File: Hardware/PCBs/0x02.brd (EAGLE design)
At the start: 99.4 x 39.4 mm, 42 parts, among them IC1 78L05Z, IC2 TL072, IC3 4050N, SW1 TL2285

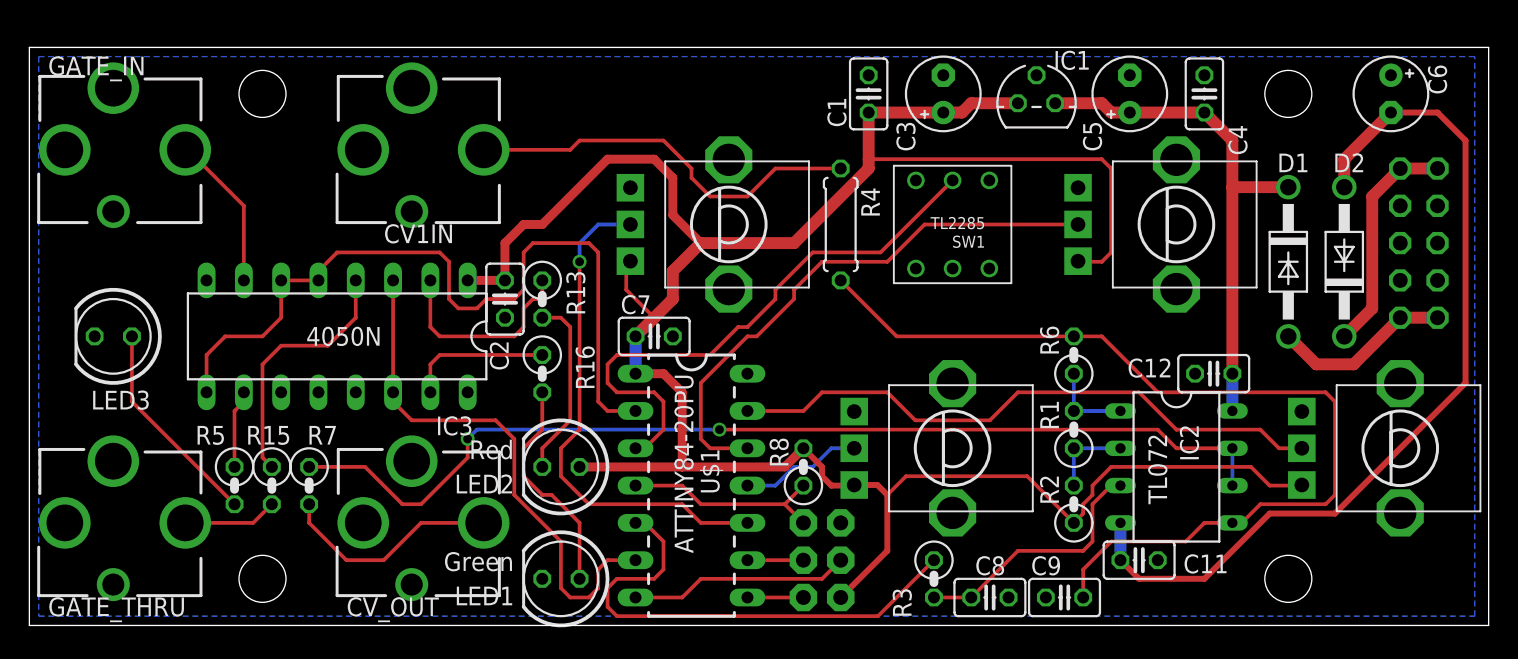
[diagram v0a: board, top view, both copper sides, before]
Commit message: Checkin of code & PCB for version 3 with DAC instead of PWM output.
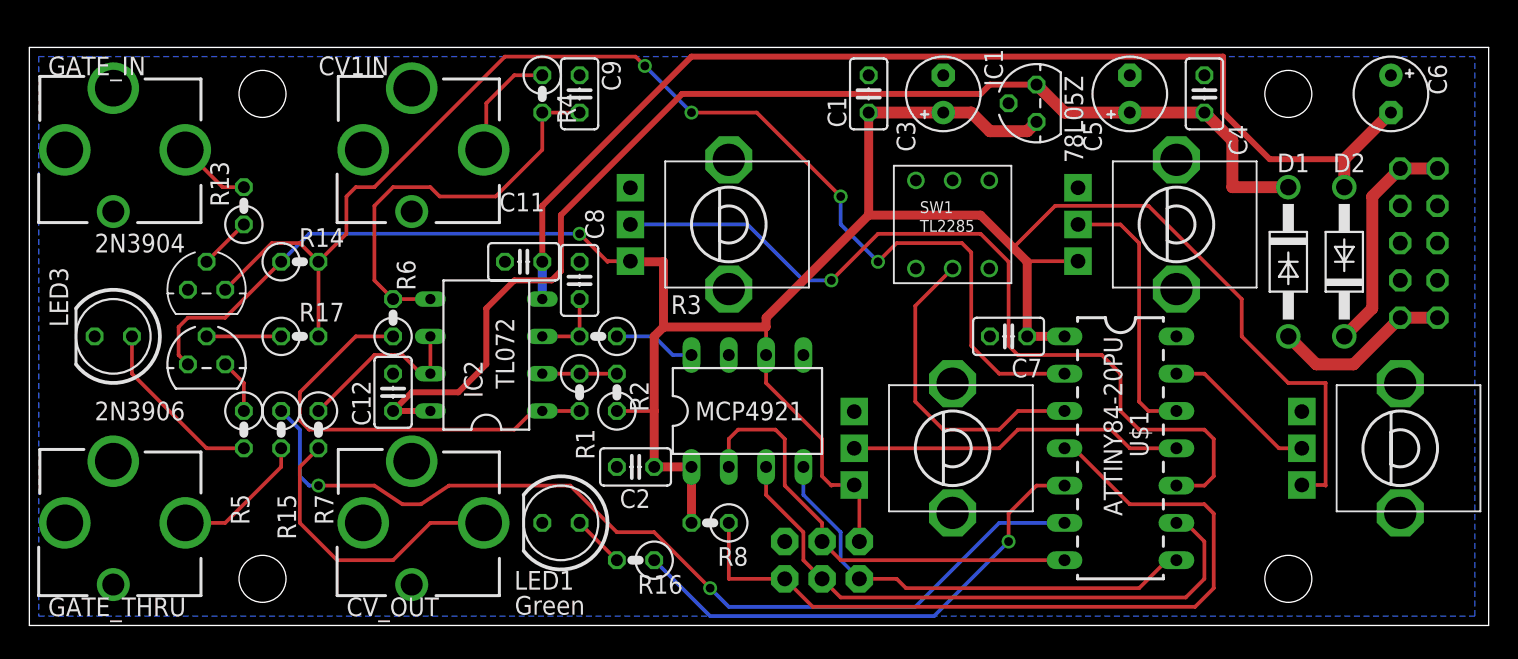
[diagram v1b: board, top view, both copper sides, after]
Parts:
- removed IC3: 4050N, 40xx:DIL16
- removed LED2: Red, led:LED5MM
- added Q1: 2N3906, transistor-pnp:TO92
- added R14: 10k, rcl:0207/2V
- added R17: 100k, rcl:0207/2V
- added T1: 2N3904, transistor:TO92
- added U$3: MCP4921, adafruit_mcp:DIL08
- C8, C9: value 10n -> 470p
- R13: value 1k -> 100k
- R4: device rcl:0207/7 -> rcl:0207/2V
- moved C12 55.9 mm to (25.4, 16.5), turned to 90 degrees
- moved C9 47.6 mm to (38.1, 36.8), turned to 90 degrees
- moved IC2 47.6 mm to (31.8, 19.1), turned to 90 degrees
- moved C11 46.6 mm to (34.3, 25.4), turned to 0 degrees
- moved R6 46.4 mm to (25.4, 21.6)
- moved C8 35.3 mm to (38.1, 24.1), turned to 90 degrees
- moved R1 33.8 mm to (38.1, 16.5), turned to 270 degrees
- moved R2 32.0 mm to (40.6, 16.5)
- moved U$1 29.3 mm to (74.9, 11.4)
- moved R3 28.2 mm to (39.4, 20.3), turned to 180 degrees
- moved C7 24.1 mm to (67.3, 20.3), turned to 180 degrees
- moved R4 22.2 mm to (35.6, 36.8)
- moved R13 21.3 mm to (15.2, 29.2), turned to 90 degrees
- moved C2 14.5 mm to (41.9, 11.4), turned to 180 degrees
- moved R16 14.2 mm to (41.9, 5.08), turned to 180 degrees
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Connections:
- removed net GATE: IC3.5, IC3.6, IC3.9, U$1.2
- removed net MISO: U$1.8, U$2.1
- removed net MOSI: U$1.7, U$2.4
- removed net N$17: IC3.4, R15.1
- removed net N$18: IC3.15, R16.1
- removed net N$20: LED2.K, R13.2
- removed net PWM_B: IC3.14, IC3.3, U$1.6
- new net DAC_OUT: R3.1, U$3.8
- new net GATE_IN: R14.2, R17.2, T1.1, U$1.2
- new net GATE_OUT: R15.1, U$1.6
- new net MISO_DO: U$1.8, U$2.1, U$3.4
- new net MOSI_SS: U$1.7, U$2.4, U$3.2
- new net N$4: Q1.2, R17.1
- net +5V: now also Q1.3, R14.1, U$3.1, U$3.6; no longer IC3.1, LED2.A
- net GND: now also T1.3, U$3.5, U$3.7; no longer IC3.11, IC3.8
- net N$1: now also T1.2; no longer IC3.2
- net N$2: now also Q1.1; no longer IC3.10
- net N$8: now also R13.2; no longer IC3.7
- net PWM_A: now also R16.1; no longer R3.1
- net SCK: now also U$3.3
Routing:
- net GATE_IN: track 0.00 -> 86.2 mm, vias 0 -> 4
- net GATE_OUT: track 0.00 -> 63.9 mm, vias 0 -> 2
- net N$15: track 69.8 -> 12.3 mm, vias 2 -> 0
- net GATE: track 53.6 -> 0.00 mm
- net +12V: track 35.3 -> 81.9 mm
- net RESET: track 14.3 -> 55.2 mm
- net SCK: track 3.81 -> 41.3 mm
- net N$12: track 64.6 -> 28.0 mm
- net PWM_B: track 36.2 -> 0.00 mm
- net MISO_DO: track 0.00 -> 31.8 mm
- net MOSI_SS: track 0.00 -> 31.3 mm
- net PA0: track 41.4 -> 10.6 mm
- net PA3: track 34.4 -> 58.6 mm
- net N$10: track 5.72 -> 29.7 mm
- net PA1: track 37.8 -> 18.3 mm
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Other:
- board text added: "0x02v3"
- board text added: "cc-by-sa 2015 Lars Bengtsson"
- board text removed: "0x02"
- board text removed: "cc-by-sa 2014 Lars Bengtsson"

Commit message: Added jumper to set voltage output range, -5V to +5V or 0-+10V.
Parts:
- added JP2: (no value), pinhead:1X03
- moved C2 1.80 mm to (43.2, 10.2), turned to 270 degrees
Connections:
- new net N$6: JP2.2, R2.1
- net +5V: now also JP2.1; no longer R2.1
- net GND: now also JP2.3
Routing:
- net N$6: track 0.00 -> 3.96 mm
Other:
- board text added: "0x02 3.1 20150320"
- board text added: "Bipolar -5V to +5V"
- board text added: "Unipolar 0V to +10V"
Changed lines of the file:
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@@
 <wire x1="92.71" y1="20.32" x2="92.71" y2="33.02" width="0.254" layer="22" style="shortdash"/>
 <rectangle x1="92.71" y1="33.02" x2="97.79" y2="33.655" layer="22"/>
+<text x="31.115" y="12.7" size="1.27" layer="22" rot="SMR90">Unipolar
+0V to +10V</text>
+<text x="90.17" y="1.905" size="1.27" layer="25">0x02 3.1
+20150320</text>
+<text x="41.91" y="12.7" size="1.27" layer="22" rot="SMR90">Bipolar
+-5V to +5V</text>
 </plain>
 <attributes>
@@
 <attribute name="VALUE" x="18.9992" y="18.0848" size="1.27" layer="27" ratio="10"/>
 </element>
-<element name="C2" library="rcl" package="C025-025X050" value="100n" x="41.91" y="11.43" smashed="yes" rot="R180">
-<attribute name="NAME" x="42.926" y="9.906" size="1.27" layer="25" ratio="10" rot="R180"/>
-<attribute name="VALUE" x="44.196" y="8.509" size="1.27" layer="27" ratio="10" rot="R180"/>
+<element name="C2" library="rcl" package="C025-025X050" value="100n" x="43.18" y="10.16" smashed="yes" rot="R270">
+<attribute name="NAME" x="42.164" y="6.604" size="1.27" layer="25" ratio="10"/>
+<attribute name="VALUE" x="40.386" y="11.176" size="1.27" layer="27" ratio="10" rot="R270"/>
+</element>
+<element name="JP2" library="pinhead" package="1X03" value="" x="38.1" y="12.7" smashed="yes" rot="MR0">
+<attribute name="NAME" x="39.4462" y="9.4488" size="1.27" layer="26" ratio="10" rot="MR0"/>
+<attribute name="VALUE" x="41.91" y="9.525" size="1.27" layer="28" rot="MR0"/>
 </element>
 </elements>
@@
 <contactref element="U$3" pad="5"/>
 <contactref element="C2" pad="2"/>
+<contactref element="JP2" pad="3"/>
 </signal>
 <signal name="+5V">
@@
 <contactref element="C7" pad="1"/>
 <contactref element="U$2" pad="2"/>
-<contactref element="R2" pad="1"/>
 <contactref element="R8" pad="2"/>
 <contactref element="R9" pad="P$1"/>
@@
 <wire x1="50.8" y1="20.955" x2="43.815" y2="20.955" width="0.6096" layer="1"/>
 <wire x1="43.815" y1="20.955" x2="43.18" y2="20.32" width="0.6096" layer="1"/>
-<wire x1="43.18" y1="20.32" x2="43.18" y2="15.24" width="0.6096" layer="1"/>
-<wire x1="43.18" y1="15.24" x2="43.18" y2="11.43" width="0.6096" layer="1"/>
+<wire x1="43.18" y1="20.32" x2="43.18" y2="12.7" width="0.6096" layer="1"/>
+<wire x1="43.18" y1="12.7" x2="43.18" y2="11.43" width="0.6096" layer="1"/>
 <wire x1="43.815" y1="20.955" x2="43.815" y2="25.4" width="0.6096" layer="1"/>
 <wire x1="43.815" y1="25.4" x2="41.6" y2="25.4" width="0.6096" layer="1"/>
@@
 <wire x1="57.15" y1="6.35" x2="57.15" y2="9.85" width="0.254" layer="1"/>
 <wire x1="57.15" y1="9.85" x2="56.8" y2="10.2" width="0.254" layer="1"/>
-<wire x1="40.64" y1="15.24" x2="43.18" y2="15.24" width="0.254" layer="1"/>
 <wire x1="64.77" y1="35.56" x2="66.04" y2="34.29" width="0.8128" layer="1"/>
 <wire x1="66.04" y1="34.29" x2="68.58" y2="34.29" width="0.8128" layer="1"/>
 <wire x1="68.58" y1="34.29" x2="69.215" y2="34.925" width="0.8128" layer="1"/>
+<contactref element="JP2" pad="1"/>
+<wire x1="40.64" y1="12.7" x2="43.18" y2="12.7" width="0.4064" layer="1"/>
 </signal>
 <signal name="MISO_DO">
@@
 <wire x1="12.7" y1="20.32" x2="17.78" y2="20.32" width="0.254" layer="1"/>
 </signal>
+<signal name="N$6">
+<contactref element="R2" pad="1"/>
+<contactref element="JP2" pad="2"/>
+<wire x1="40.64" y1="15.24" x2="40.005" y2="15.24" width="0.4064" layer="1"/>
+<wire x1="40.005" y1="15.24" x2="38.1" y2="13.335" width="0.4064" layer="1"/>
+<wire x1="38.1" y1="13.335" x2="38.1" y2="12.7" width="0.4064" layer="1"/>
+</signal>
 </signals>

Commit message: Make voltage mixer into a true voltage adder (ext cv in tied to GND when unused, and 2x gain in output amp).
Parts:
- added R18, R19: 100k, rcl:0207/2V
- moved R6 1.80 mm to (24.1, 20.3), turned to 0 degrees
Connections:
- new net N$13: IC2.6, R18.1, R19.2
- net GND: now also CV1IN.2, R19.1
- net N$15: now also R18.2; no longer IC2.6
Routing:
- net N$13: track 0.00 -> 10.8 mm
- net N$15: track 12.3 -> 16.6 mm
- net N$12: track 28.0 -> 30.6 mm
- net N$10: track 29.7 -> 27.1 mm
- net GATE_IN: track 86.2 -> 84.9 mm
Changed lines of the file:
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@@
 </element>
 <element name="R4" library="rcl" package="0207/2V" value="100k" x="35.56" y="36.83" rot="R270"/>
-<element name="R6" library="rcl" package="0207/2V" value="100k" x="25.4" y="21.59" smashed="yes" rot="R90">
-<attribute name="NAME" x="26.924" y="23.4442" size="1.27" layer="25" ratio="10" rot="R90"/>
-<attribute name="VALUE" x="25.0952" y="23.4442" size="1.27" layer="27" ratio="10" rot="R90"/>
+<element name="R6" library="rcl" package="0207/2V" value="100k" x="24.13" y="20.32" smashed="yes">
+<attribute name="NAME" x="20.9042" y="17.526" size="1.27" layer="25" ratio="10"/>
+<attribute name="VALUE" x="21.5392" y="21.8948" size="1.27" layer="27" ratio="10"/>
 </element>
 <element name="R7" library="rcl" package="0207/2V" value="1k" x="20.32" y="13.97" smashed="yes" rot="R270">
@@
 <element name="R13" library="rcl" package="0207/2V" value="100k" x="15.24" y="29.21" rot="R90"/>
 <element name="R14" library="rcl" package="0207/2V" value="10k" x="19.05" y="25.4" smashed="yes">
-<attribute name="NAME" x="18.9992" y="26.416" size="1.27" layer="25" ratio="10"/>
-<attribute name="VALUE" x="18.9992" y="28.2448" size="1.27" layer="27" ratio="10"/>
+<attribute name="NAME" x="18.3642" y="26.416" size="1.27" layer="25" ratio="10"/>
+<attribute name="VALUE" x="18.3642" y="28.2448" size="1.27" layer="27" ratio="10"/>
 </element>
 <element name="U$3" library="adafruit_mcp" package="DIL08" value="MCP4921" x="49.53" y="15.24" smashed="yes">
@@
 </element>
 <element name="R17" library="rcl" package="0207/2V" value="100k" x="19.05" y="20.32" smashed="yes">
-<attribute name="NAME" x="18.9992" y="21.336" size="1.27" layer="25" ratio="10"/>
-<attribute name="VALUE" x="18.9992" y="18.0848" size="1.27" layer="27" ratio="10"/>
+<attribute name="NAME" x="16.4592" y="17.526" size="1.27" layer="25" ratio="10"/>
+<attribute name="VALUE" x="15.8242" y="21.8948" size="1.27" layer="27" ratio="10"/>
 </element>
 <element name="C2" library="rcl" package="C025-025X050" value="100n" x="43.18" y="10.16" smashed="yes" rot="R270">
@@
 <attribute name="NAME" x="39.4462" y="9.4488" size="1.27" layer="26" ratio="10" rot="MR0"/>
 <attribute name="VALUE" x="41.91" y="9.525" size="1.27" layer="28" rot="MR0"/>
+</element>
+<element name="R18" library="rcl" package="0207/2V" value="100k" x="24.13" y="25.4" smashed="yes" rot="R180">
+<attribute name="NAME" x="22.8092" y="26.416" size="1.27" layer="25" ratio="10"/>
+<attribute name="VALUE" x="22.1742" y="28.2448" size="1.27" layer="27" ratio="10"/>
+</element>
+<element name="R19" library="rcl" package="0207/2V" value="100k" x="29.21" y="25.4" smashed="yes" rot="R180">
+<attribute name="NAME" x="27.8892" y="26.416" size="1.27" layer="25" ratio="10"/>
+<attribute name="VALUE" x="27.8892" y="28.8798" size="1.27" layer="27" ratio="10"/>
 </element>
 </elements>
@@
 <contactref element="C2" pad="2"/>
 <contactref element="JP2" pad="3"/>
+<contactref element="CV1IN" pad="2"/>
+<contactref element="R19" pad="1"/>
 </signal>
 <signal name="+5V">
@@
 <wire x1="19.05" y1="14.605" x2="19.05" y2="16.51" width="0.254" layer="1"/>
 <wire x1="19.05" y1="16.51" x2="22.86" y2="20.32" width="0.254" layer="1"/>
-<wire x1="22.86" y1="20.32" x2="25.4" y2="20.32" width="0.254" layer="1"/>
 <wire x1="38.1" y1="15.24" x2="35.56" y2="15.24" width="0.254" layer="1"/>
 </signal>
@@
 <wire x1="27.94" y1="30.48" x2="25.4" y2="30.48" width="0.254" layer="1"/>
 <wire x1="25.4" y1="30.48" x2="24.13" y2="29.21" width="0.254" layer="1"/>
-<wire x1="24.13" y1="29.21" x2="24.13" y2="24.13" width="0.254" layer="1"/>
-<wire x1="24.13" y1="24.13" x2="25.4" y2="22.86" width="0.254" layer="1"/>
-<wire x1="25.4" y1="22.86" x2="27.94" y2="22.86" width="0.254" layer="1"/>
+<wire x1="27.94" y1="22.86" x2="25.4" y2="22.86" width="0.254" layer="1"/>
+<wire x1="25.4" y1="22.86" x2="24.13" y2="24.13" width="0.254" layer="1"/>
+<wire x1="24.13" y1="24.13" x2="24.13" y2="29.21" width="0.254" layer="1"/>
+<wire x1="25.4" y1="22.86" x2="25.4" y2="20.32" width="0.254" layer="1"/>
 </signal>
 <signal name="N$14">
@@
 <contactref element="IC2" pad="7"/>
 <contactref element="R7" pad="1"/>
-<contactref element="IC2" pad="6"/>
 <wire x1="27.94" y1="17.78" x2="27.305" y2="17.78" width="0.254" layer="1"/>
 <wire x1="27.305" y1="17.78" x2="26.035" y2="19.05" width="0.254" layer="1"/>
 <wire x1="26.035" y1="19.05" x2="24.13" y2="19.05" width="0.254" layer="1"/>
 <wire x1="24.13" y1="19.05" x2="20.32" y2="15.24" width="0.254" layer="1"/>
-<wire x1="27.94" y1="17.78" x2="27.94" y2="20.32" width="0.254" layer="1"/>
+<contactref element="R18" pad="2"/>
+<wire x1="22.86" y1="25.4" x2="22.86" y2="22.86" width="0.254" layer="1"/>
+<wire x1="22.86" y1="22.86" x2="24.13" y2="21.59" width="0.254" layer="1"/>
+<wire x1="24.13" y1="21.59" x2="24.13" y2="19.05" width="0.254" layer="1"/>
 </signal>
 <signal name="N$11">
@@
 <contactref element="R17" pad="2"/>
 <wire x1="13.97" y1="23.495" x2="17.145" y2="26.67" width="0.254" layer="1"/>
-<wire x1="17.145" y1="26.67" x2="19.05" y2="26.67" width="0.254" layer="1"/>
-<wire x1="19.05" y1="26.67" x2="20.32" y2="25.4" width="0.254" layer="1"/>
+<wire x1="17.145" y1="26.67" x2="20.32" y2="26.67" width="0.254" layer="1"/>
 <wire x1="20.32" y1="20.32" x2="20.32" y2="25.4" width="0.254" layer="1"/>
-<wire x1="20.32" y1="25.4" x2="22.225" y2="27.305" width="0.254" layer="1"/>
-<wire x1="22.225" y1="27.305" x2="22.225" y2="29.845" width="0.254" layer="1"/>
-<wire x1="22.225" y1="29.845" x2="22.86" y2="30.48" width="0.254" layer="1"/>
-<wire x1="22.86" y1="30.48" x2="24.13" y2="30.48" width="0.254" layer="1"/>
-<wire x1="24.13" y1="30.48" x2="33.02" y2="39.37" width="0.254" layer="1"/>
+<wire x1="20.32" y1="25.4" x2="20.32" y2="26.67" width="0.254" layer="1"/>
+<wire x1="20.32" y1="26.67" x2="33.02" y2="39.37" width="0.254" layer="1"/>
 <wire x1="33.02" y1="39.37" x2="41.91" y2="39.37" width="0.254" layer="1"/>
 <wire x1="41.91" y1="39.37" x2="42.545" y2="38.735" width="0.254" layer="1"/>
@@
 <wire x1="38.1" y1="13.335" x2="38.1" y2="12.7" width="0.4064" layer="1"/>
 </signal>
+<signal name="N$13">
+<contactref element="IC2" pad="6"/>
+<contactref element="R18" pad="1"/>
+<contactref element="R19" pad="2"/>
+<wire x1="25.4" y1="25.4" x2="27.94" y2="25.4" width="0.254" layer="1"/>
+<wire x1="27.94" y1="20.32" x2="29.845" y2="20.32" width="0.254" layer="1"/>
+<wire x1="29.845" y1="20.32" x2="30.48" y2="20.955" width="0.254" layer="1"/>
+<wire x1="30.48" y1="20.955" x2="30.48" y2="22.86" width="0.254" layer="1"/>
+<wire x1="30.48" y1="22.86" x2="27.94" y2="25.4" width="0.254" layer="1"/>
+</signal>
 </signals>
